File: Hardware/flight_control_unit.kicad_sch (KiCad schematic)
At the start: 36 parts, among them SW3 SW_SPDT, SW4 SW_Push_Dual, U12 STM32F405RGTx, Y2 25MHz

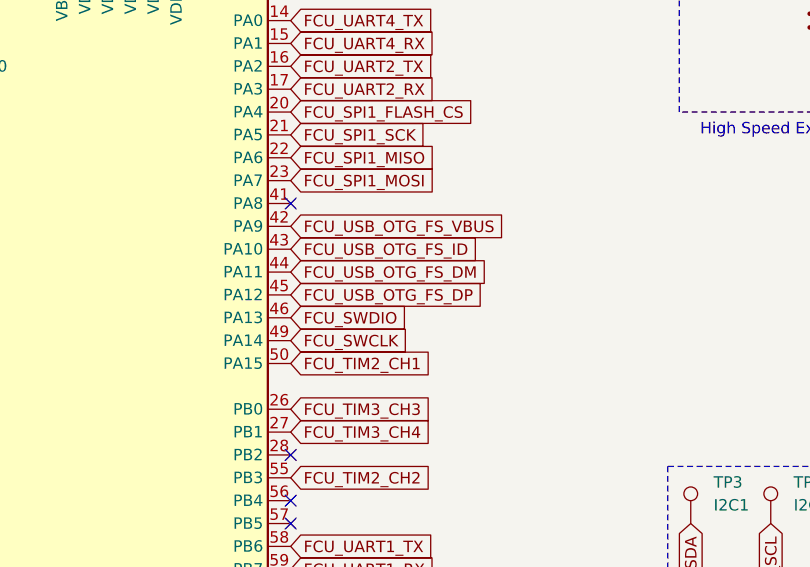
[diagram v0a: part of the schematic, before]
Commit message: hardware: better layout, no power supply and sensors
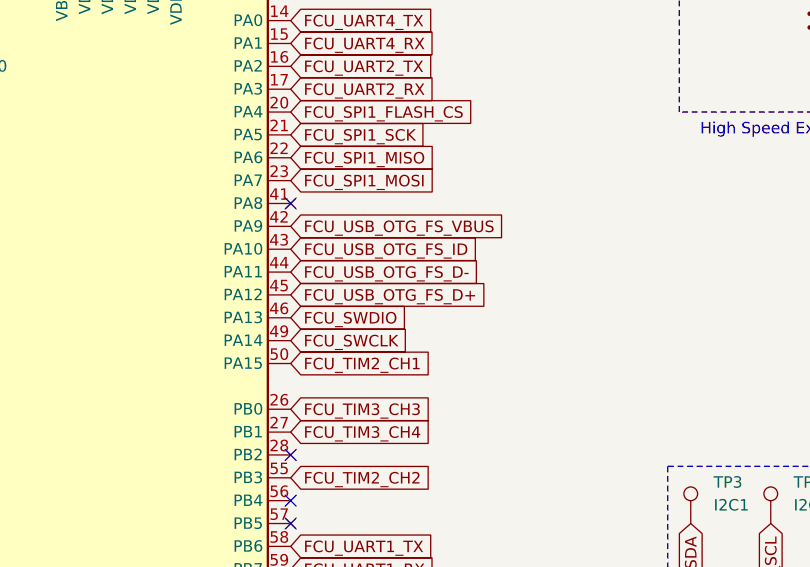
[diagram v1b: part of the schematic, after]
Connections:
- net FCU_USB_OTG_FS_DM renamed FCU_USB_OTG_FS_D-
- net FCU_USB_OTG_FS_DP renamed FCU_USB_OTG_FS_D+
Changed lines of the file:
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@@
 		)
 	)
-	(global_label "FCU_USB_OTG_FS_DP"
+	(global_label "FCU_USB_OTG_FS_D+"
 		(shape input)
 		(at 87.63 101.6 0)
@@
 		)
 		(property "Intersheetrefs" "${INTERSHEET_REFS}"
-			(at 110.3909 101.6 0)
+			(at 110.6933 101.6 0)
 			(effects
 				(font
@@
 		)
 	)
-	(global_label "FCU_USB_OTG_FS_DM"
+	(global_label "FCU_USB_OTG_FS_D-"
 		(shape input)
 		(at 87.63 99.06 0)
@@
 		)
 		(property "Intersheetrefs" "${INTERSHEET_REFS}"
-			(at 110.5723 99.06 0)
-			(effects
-				(font
+			(at 110.6933 99.06 0)
+			(effects
+				(font
